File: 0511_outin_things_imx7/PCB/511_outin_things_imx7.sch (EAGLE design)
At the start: 52 parts

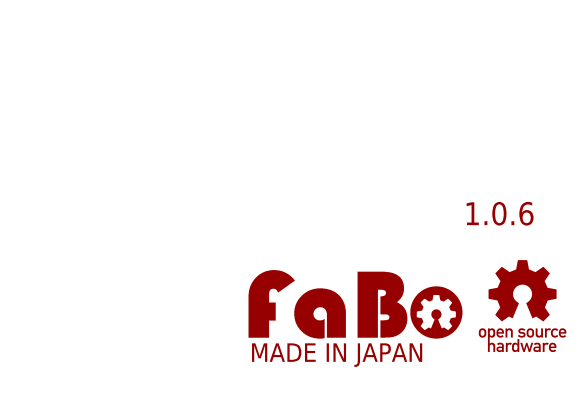
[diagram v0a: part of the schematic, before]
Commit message: #511 outin_things_imx7　ロゴ修正
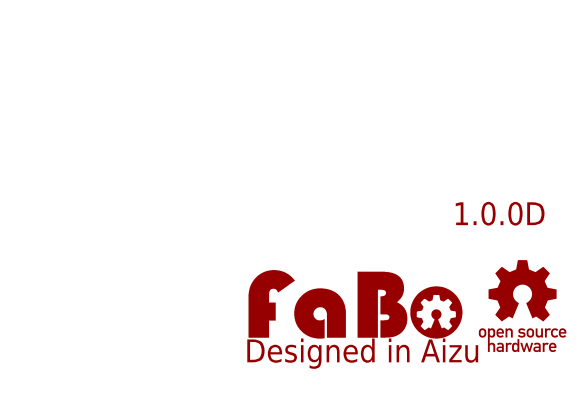
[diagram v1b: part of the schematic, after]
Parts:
- removed U$14: (no value), FaBo-etc:LOGO_FABO-M
- added LOGO1: (no value), component:LOGO_FABO-M
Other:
- note added: "1.0.0D"
- note removed: "1.0.6"
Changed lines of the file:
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@@
 <?xml version="1.0" encoding="utf-8"?>
 <!DOCTYPE eagle SYSTEM "eagle.dtd">
-<eagle version="9.2.2">
+<eagle version="9.6.2">
 <drawing>
 <settings>
@@
 <setting verticaltext="up"/>
 </settings>
-<grid distance="0.1" unitdist="inch" unit="inch" style="lines" multiple="1" display="no" altdistance="0.01" altunitdist="inch" altunit="inch"/>
+<grid distance="0.1" unitdist="inch" unit="inch" style="lines" multiple="1" display="yes" altdistance="0.01" altunitdist="inch" altunit="inch"/>
 <layers>
 <layer number="1" name="Top" color="4" fill="1" visible="no" active="no"/>
@@
 <layer number="59" name="tCarbon" color="7" fill="1" visible="no" active="no"/>
 <layer number="60" name="bCarbon" color="7" fill="1" visible="no" active="no"/>
+<layer number="88" name="SimResults" color="9" fill="1" visible="no" active="no"/>
+<layer number="89" name="SimProbes" color="9" fill="1" visible="no" active="no"/>
 <layer number="90" name="Modules" color="5" fill="1" visible="yes" active="yes"/>
 <layer number="91" name="Nets" color="2" fill="1" visible="yes" active="yes"/>
@@
 <layer number="112" name="tSilk" color="7" fill="1" visible="yes" active="yes"/>
 <layer number="113" name="IDFDebug" color="4" fill="1" visible="yes" active="yes"/>
+<layer number="114" name="sd0" color="7" fill="1" visible="no" active="no"/>
 <layer number="115" name="sd" color="13" fill="1" visible="yes" active="yes"/>
 <layer number="116" name="Patch_BOT" color="9" fill="4" visible="no" active="yes"/>
+<layer number="117" name="BACKMAAT1" color="7" fill="1" visible="no" active="no"/>
 <layer number="118" name="Rect_Pads" color="7" fill="1" visible="no" active="no"/>
+<layer number="119" name="KAP_TEKEN" color="7" fill="1" visible="no" active="no"/>
+<layer number="120" name="KAP_MAAT1" color="7" fill="1" visible="no" active="no"/>
 <layer number="121" name="_tsilk" color="7" fill="1" visible="no" active="yes"/>
 <layer number="122" name="_bsilk" color="7" fill="1" visible="no" active="yes"/>
@@
 <layer number="128" name="_bValues" color="7" fill="1" visible="yes" active="yes"/>
 <layer number="129" name="Mask" color="7" fill="1" visible="yes" active="yes"/>
+<layer number="130" name="SMDSTROOK" color="7" fill="1" visible="no" active="no"/>
 <layer number="131" name="tAdjust" color="7" fill="1" visible="no" active="yes"/>
 <layer number="132" name="bAdjust" color="7" fill="1" visible="no" active="yes"/>
+<layer number="133" name="bottom_silk" color="7" fill="1" visible="no" active="no"/>
+<layer number="134" name="silk_top" color="7" fill="1" visible="no" active="no"/>
+<layer number="135" name="silk_bottom" color="7" fill="1" visible="no" active="no"/>
+<layer number="136" name="silktop" color="7" fill="1" visible="no" active="no"/>
+<layer number="137" name="silkbottom" color="7" fill="1" visible="no" active="no"/>
+<layer number="138" name="EEE" color="7" fill="1" visible="no" active="no"/>
+<layer number="139" name="_tKeepout" color="7" fill="1" visible="no" active="no"/>
+<layer number="141" name="ASSEMBLY_TOP" color="7" fill="1" visible="no" active="no"/>
+<layer number="143" name="PLACE_BOUND_TOP" color="7" fill="1" visible="no" active="no"/>
 <layer number="144" name="Drill_legend" color="7" fill="1" visible="no" active="yes"/>
+<layer number="145" name="DrillLegend_01-16" color="7" fill="1" visible="no" active="no"/>
+<layer number="146" name="DrillLegend_01-20" color="7" fill="1" visible="no" active="no"/>
+<layer number="147" name="PIN_NUMBER" color="7" fill="1" visible="no" active="no"/>
 <layer number="150" name="Notes" color="7" fill="1" visible="no" active="yes"/>
 <layer number="151" name="HeatSink" color="7" fill="1" visible="no" active="yes"/>
@@
 </classes>
 <parts>
-<part name="U$14" library="FaBo-etc" deviceset="LOGO_FABO" device="-M"/>
 <part name="U1" library="FaBo-Boards" deviceset="RASPBERRY_PI_B+" device=""/>
 <part name="SUPPLY2" library="FaBo-etc" deviceset="5V" device=""/>
@@
 <part name="I2S_OUT" library="FaBo-Template" deviceset="FABO_BRICK_I2S" device="TOP"/>
 <part name="I2S_IN" library="FaBo-Template" deviceset="FABO_BRICK_I2S" device="TOP"/>
+<part name="LOGO1" library="component" deviceset="LOGO_FABO" device="-M"/>
 </parts>
 <sheets>
 <sheet>
 <plain>
-<text x="373.38" y="20.32" size="2.54" layer="94" align="bottom-center">1.0.6</text>
+<text x="373.38" y="20.32" size="2.54" layer="94" align="bottom-center">1.0.0D</text>
 <text x="162.56" y="243.84" size="2.54" layer="97">GPIO (3pin Side 2mm pitch) x4</text>
 <text x="17.78" y="55.88" size="2.54" layer="97">I2C(4pin Side 2mm pitch) x3</text>
@@
 </plain>
 <instances>
-<instance part="U$14" gate="G$1" x="345.44" y="5.08" smashed="yes"/>
 <instance part="U1" gate="G$1" x="45.72" y="203.2" smashed="yes">
 <attribute name="NAME" x="33.02" y="231.648" size="1.778" layer="95"/>
@@
 <attribute name="NAME" x="68.072" y="53.34" size="1.778" layer="95" rot="R90"/>
 </instance>
+<instance part="LOGO1" gate="G$1" x="345.44" y="5.08" smashed="yes"/>
 </instances>
 <busses>
